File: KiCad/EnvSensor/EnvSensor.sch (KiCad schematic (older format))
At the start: 57 parts

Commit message: Schematic done
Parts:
- removed D?: WS2812B, LED_SMD:LED_WS2812B_PLCC4_5.0x5.0mm_P3.2mm, symbol LED:WS2812B
- added BZ?: Buzzer, symbol Device:Buzzer
- added C? (x2): 1u, symbol Device:C
- added C? (x4): 100n, symbol Device:C
- added D?: GREEN_LED, symbol Device:LED
- added Q?: IRLML2502, Package_TO_SOT_SMD:SOT-23, symbol Transistor_FET:IRLML2060
- added R?: 10, symbol Device:R
- added R? (x5): 100k, symbol Device:R
- added R?: 1m, symbol Device:R
- added R?: 2k2, symbol Device:R
- added R? (x4): 10k, symbol Device:R
- added SW? (x4): SW_Push, symbol Switch:SW_Push
- added U?: TPS782-DDC, Package_TO_SOT_SMD:SOT-23-5, symbol myLib:TPS782-DDC
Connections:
- net +3V3: now also BZ?.1 (-), J?.4 (VDD), U?.1 (VDD), U?.8 (VCC), R?.1, R?.1, R?.1, R?.1; no longer U?.1 (VDD)
- net +BATT: now also C?.1, U?.1 (VIN)
- net GND: now also J?.6 (VSS), U?.2 (GND), U?.9 (GND), C?.2, C?.2, C?.2, C?.2, C?.2, C?.2, Q?.2 (S), R?.2, R?.2, R?.2, SW?.1, SW?.1, SW?.1, SW?.1
- net MOSI: now reaches U?.3 (DIN)
- net MOSI: now also J?.3 (CMD)
- net SCK: now reaches U?.4 (CLK)
- net SCK: now also J?.5 (CLK)
- net E_INK_SELECT: now reaches U?.5 (CS)
- net E_INK_CD: now reaches U?.6 (DC)
- net E_INK_RESET: now reaches U?.7 (RST)
- net E_INK_BUSY: now reaches U?.8 (BUSY)
- net BUZZ_DAC: now reaches U?.15 (PA5)
- net at BZ?.2 (+): now also R?.1
- net SD_CS: now reaches J?.2 (DAT3/CD)
- net MISO: now reaches J?.7 (DAT0)
- net WIFI_RESET: now reaches U?.1 (Reset)
- net WIFI_RX: now reaches U?.15 (RXD0)
- net WIFI_TX: now reaches U?.16 (TXD0)
- net WIFI_ENABLE: now reaches U?.3 (EN)
- new net: Q?.3 (D), R?.2
- new net: D?.1 (K), R?.1
- new net: R?.2, R?.2, SW?.2 (x4)
- new net +3.3VP: C?.1, U?.1 (VDD), U?.5 (VOUT)
- new net AUX_POWER_ENABLE: R?.1, U?.3 (EN)
- new net BUZZ_SWITCH: Q?.1 (G), R?.1
- new net LED: D?.2 (A)
- new net SWITCH_1: C?.1, R?.1
- new net SWITCH_2: C?.1, R?.1
- new net SWITCH_3: C?.1, R?.1
- new net SWITCH_4: C?.1, R?.1
- no-connect marks 1 -> 13
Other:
- note added: "I(led)=1mA\nR=(3.3V-1.8V)/1mA\nR=1k5"
- note added: "SCD30 C02 sensor\n3.3-5.5V\n1-75mA, 20mA avg"
- note added: "STM32L431CCTx | MTU | | 1.71-3.6 V\nUSB connectivity?\n\nMCP73832 | USB Battery charger\nAP9101 | Battery protection\nTPS782 | 500-nA IQ,150-mA, Ultra-Low Quiescent Current\nLow-Dropout Linear Regulator\n\nSCD30 | C02 sensor | I2C 0xC2 | 3.3-5.5VV / 1-65mA, 20mA avg\nHIH8121 | Humidity | I2c 0x27 | 2.3-5.5V / 1mA\nBME280 | Pressure | I2C 0x76/0x77 | 1.7-3.6V\nSSD1306 | Display | I2C 0x3C << 1 | 3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"
- note added: "TPS782 LDO\nDropout 135-175mV\nImax 150-mA\n500-nA Quiescent Current\n"
- note added: "WiFi Module"
- note removed: "SCD30 C02 sensor\n"
- note removed: "STM32L431CCTx | MTU | | 1.71-3.6 V\nUSB connectivity?\n\nMCP73832 | USB Battery charger\nAP9101 | Battery protection\nTPS782 | 500-nA IQ,150-mA, Ultra-Low Quiescent Current\nLow-Dropout Linear Regulator\n\nSCD30 | C02 sensor | I2C 0xC2 | 3.3-5.5VV / 20mA\nHIH8121 | Humidity | I2c 0x27 | 2.3-5.5V / 1mA\nBME280 | Pressure | I2C 0x76/0x77 | 1.7-3.6V\nSSD1306 | Display | I2C 0x3C << 1 | 3.3V\n | Ink 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"
- note removed: "TPS782 LDO\n135-175mV\n150-mA\n500-nA Quiescent Current\n"
- moved on the sheet: BZ?, C?, D?, F?, J?, L?, Q?, Q?A, Q?B, R?, U?, Y?

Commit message: Some commit
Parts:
- removed BZ?: Buzzer, symbol Device:Buzzer
- removed F?: 1812L200/12DR, symbol Device:Polyfuse
- removed Q? (x2): Si7252DP, symbol myLib:Si7252DP
- removed U?: USBLC6-2SC6, Package_TO_SOT_SMD:SOT-23-6, symbol Power_Protection:USBLC6-2SC6
- removed U?: STM32L475RCT6, Package_QFP:LQFP-64_10x10mm_P0.5mm, symbol MCU_ST_STM32L4:STM32L475RCTx
- added BT1, BT2, BT3: Li-Ion, JPConnectors:BatteryHolder_Keystone_1042_1x18650, symbol Device:Battery_Cell
- added C26, C27: 15p, Capacitor_SMD:C_0805_2012Metric, symbol Device:C
- added D5: GREEN_LED, LED_THT:LED_D3.0mm, symbol Device:LED
- added D6, D7: RED LED, LED_THT:LED_D3.0mm_Horizontal_O3.81mm_Z10.0mm, symbol Device:LED
- added H1, H2, H3, H4: MountingHole, MountingHole:MountingHole_3.2mm_M3, symbol Mechanical:MountingHole
- added Q3: SQJB80EP, Package_SO:PowerPAK_SO-8_Dual, symbol myLib:SQJB80EP
- added Y2: 32768/12.5pF, Crystal:Crystal_SMD_MicroCrystal_CC7V-T1A-2Pin_3.2x1.5mm, symbol Device:Crystal_Small
- BZ1: renamed from BZ?; footprint (none) -> JPBuzzers:Laudity_SPB45
- C1, C2: renamed from C?; value 100n -> 6p; footprint (none) -> Capacitor_SMD:C_0805_2012Metric
- C10, C13, C14, C16, C19, C20, C3, C6, C7, C8, C9: renamed from C?; footprint (none) -> Capacitor_SMD:C_0603_1608Metric
- C11, C12, C17, C18, C21, C22, C23, C24, C25, C4: renamed from C?; footprint (none) -> Capacitor_SMD:C_0805_2012Metric
- C15: renamed from C?; value 10n -> 100n; footprint (none) -> Capacitor_SMD:C_0603_1608Metric
- C5: renamed from C?; value 100n -> 10n; footprint (none) -> Capacitor_SMD:C_0805_2012Metric
- D1, D3, D4: renamed from D?; footprint (none) -> LED_SMD:LED_0805_2012Metric
- D2: renamed from D?; value D -> MBRS260T3G; footprint (none) -> Diode_SMD:D_SMB
- J1: renamed from J?; footprint (none) -> Connector_PinHeader_2.54mm:PinHeader_1x06_P2.54mm_Horizontal
- J2: renamed from J?; footprint (none) -> Connector_PinSocket_2.54mm:PinSocket_1x04_P2.54mm_Vertical
- J3: renamed from J?; footprint (none) -> Connector_USB:USB_Micro-B_Molex_47346-0001
- J4: renamed from J?; footprint (none) -> JPConnectors:PowerSocketSMD
- J5: renamed from J?; footprint (none) -> Connector_Card:microSD_HC_Hirose_DM3AT-SF-PEJM5
- L1: renamed from L?; value L_Small -> 10u; footprint (none) -> Inductor_SMD:L_0805_2012Metric
- P1: renamed from P?; footprint (none) -> Connector_USB:USB_C_Receptacle_Amphenol_12401610E4-2A
- R1, R11, R14, R16, R20, R3, R4, R8: renamed from R?; footprint (none) -> Resistor_SMD:R_0805_2012Metric
- R10, R12, R13, R15, R18, R19, R2, R6, R7, R9: renamed from R?; footprint (none) -> Resistor_SMD:R_0603_1608Metric
- R17: renamed from R?; footprint (none) -> Resistor_SMD:R_2512_6332Metric
- R21: renamed from R?; value 1m -> 300k; footprint (none) -> Resistor_SMD:R_0805_2012Metric
- R5: renamed from R?; value 10 -> 100; footprint (none) -> Resistor_SMD:R_0805_2012Metric
- SW1, SW2, SW3, SW4: renamed from SW?; footprint (none) -> Button_Switch_SMD:SW_SPST_PTS645
- U1: renamed from U?; value STM32L431CCTx -> STM32L431CCT6
- U10: renamed from U?; footprint (none) -> JPSensors:BME280-Module
- U11: renamed from U?; footprint (none) -> JPDisplays:4.2inch_E-Ink
- U2: renamed from U?; footprint (none) -> Package_SO:MSOP-8_3x3mm_P0.65mm
- U5: renamed from U?; footprint (none) -> JPSensors:SCD30
- U8: renamed from U?; footprint (none) -> Connector_PinHeader_1.27mm:PinHeader_1x04_P1.27mm_Vertical
- U9: renamed from U?; footprint (none) -> JPComms:ESP-12S
- Y1: renamed from Y?; footprint (none) -> Crystal:Crystal_SMD_Abracon_ABM3B-4Pin_5.0x3.2mm
- gave numbers to parts that had none: 6
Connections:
- net BUZZ_DAC is gone; now on net E_INK_RESET: U1.15 (PA5)
- net +3V3: now also U4.6 (VDDIO), U4.8 (VDD); no longer U4.1 (GND), U4.7 (GND)
- net +BATT: now also BT1.1 (+), BT2.1 (+), BT3.1 (+)
- net -BATT: now also BT1.2 (-), BT2.2 (-), BT3.2 (-), Q3.3 (S2)
- net AUX_POWER_ENABLE: now also U1.33 (PA12)
- net BUZZ_SWITCH: now also U1.25 (PB12)
- net E_INK_BUSY: now also U1.16 (PA6)
- net E_INK_CD: now also U1.14 (PA4)
- net E_INK_SELECT: now also U1.13 (PA3)
- net GND: now also U1.44 (PH3), U4.1 (GND), U4.7 (GND), U6.2 (GND), U6.4 (GND), U7.2 (GND), U7.4 (GND), C26.2, C27.2, Q3.1 (S2); no longer U4.6 (VDDIO), U4.8 (VDD)
- net LED: now also U1.22 (PB11), D5.2 (A)
- net MISO: now also U1.27 (PB14)
- net MOSI: now also U1.28 (PB15)
- net SCD30_READY: now also U1.32 (PA11)
- net SCK: now also U1.26 (PB13)
- net SCL: now also U1.30 (PA9), U4.4 (SCK); no longer U4.3 (SDI)
- net SDA: now also U1.31 (PA10), U4.3 (SDI); no longer U4.4 (SCK)
- net SD_CS: now also U1.29 (PA8)
- net SWITCH_1: now also U1.17 (PA7)
- net SWITCH_2: now also U1.18 (PB0)
- net SWITCH_3: now also U1.19 (PB1)
- net SWITCH_4: now also U1.20 (PB2)
- net VBUS: now also D2.2 (A), D7.2 (A)
- net WIFI_ENABLE: now also U1.46 (PB9)
- net WIFI_RESET: now also U1.45 (PB8)
- net WIFI_RX: now also U1.42 (PB6)
- net WIFI_TX: now also U1.43 (PB7)
- net at U1.3 (PC14): now also C26.1, Y2.1
- net at U1.4 (PC15): now also C27.1, Y2.2
- net at U3.4 (DO): now also Q3.4 (G2)
- net at U3.5 (CO): now also Q3.2 (G2)
- net at P1.A6 (D+): no longer J3.3 (D+)
- net at P1.A7 (D-): no longer J3.2 (D-)
- net at C11.1, D2.1 (K), D3.2 (A)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: now also D6.2 (A)
- net at D4.1 (K), R20.2: now also D7.1 (K)
- net at D3.1 (K), R11.2: now also D6.1 (K)
- net at D1.1 (K), R4.1: now also D5.1 (K)
- new net: Q3.5 (D2), Q3.6 (D2)
- no-connect marks 13 -> 30
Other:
- note added: "Boot?"
- note added: "C1/2 = 2C(L) - 10p\nC(L)=12.5p -> C1/2=15p\nC(L)=9p -> C1/2=8p\nC(L)=7p -> C1/2=4p\n"
- note added: "I(buzz)=5mA\nRmax=3.3V/5mA\nRmax=660"
- note added: "Settings\n+\n-\nAlarm\nPower save mode\nTrigger gps"
- note added: "TPS782 LDO\nDropout 135-175mV\nImax 150-mA\n500-nA Quiescent Current"
- note added: "deltaT=(5.0V-0.5V-3.3V)*65mA*193C/W\ndeltaT=78mW*193C/W=15C"
- note removed: "TPS782 LDO\nDropout 135-175mV\nImax 150-mA\n500-nA Quiescent Current\n"
- moved on the sheet: BZ1, C1, C10, C12, C15, C2, C4, C5, C6, C7, C9, D1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

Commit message: Last pcb fixes
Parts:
- P1: footprint Connector_USB:USB_C_Receptacle_Amphenol_12401610E4-2A -> JPConnectors:USB_C_Receptacle_Adam_Tech
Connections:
- net VBUS: no longer D4.2 (A), D7.2 (A)
- net at C11.1, D2.1 (K), D3.2 (A)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: now also D4.2 (A), D7.2 (A)
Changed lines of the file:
@@
 F 0 "P1" H 1807 3467 50  0000 C CNN
 F 1 "USB_C_Plug_USB2.0" H 1807 3376 50  0000 C CNN
-F 2 "Connector_USB:USB_C_Receptacle_Amphenol_12401610E4-2A" H 1850 2600 50  0001 C CNN
+F 2 "JPConnectors:USB_C_Receptacle_Adam_Tech" H 1850 2600 50  0001 C CNN
 F 3 "https://www.usb.org/sites/default/files/documents/usb_type-c.zip" H 1850 2600 50  0001 C CNN
 	1    1700 2600
@@
 $EndComp
 $Comp
-L power:VBUS #PWR0110
-U 1 1 5F7F80CF
-P 7150 4850
-F 0 "#PWR0110" H 7150 4700 50  0001 C CNN
-F 1 "VBUS" H 7165 5023 50  0000 C CNN
-F 2 "" H 7150 4850 50  0001 C CNN
-F 3 "" H 7150 4850 50  0001 C CNN
-	1    7150 4850
-	0    1    1    0
-$EndComp
-$Comp
 L Device:C C11
 U 1 1 5F7F94C0
@@
 	4600 3950 4900 3950
 Wire Wire Line
-	4900 3950 4900 4700
+	4900 3950 4900 4150
 Connection ~ 4900 3950
 Wire Wire Line
@@
 Wire Wire Line
 	7100 4700 7050 4700
-Connection ~ 7100 4850
-Wire Wire Line
-	7100 4850 7150 4850
 Wire Wire Line
 	9700 2250 9700 2300
@@
 Text Notes 10650 3800 0    50   ~ 0
 deltaT=(5.0V-0.5V-3.3V)*65mA*193C/W\ndeltaT=78mW*193C/W=15C
+Wire Wire Line
+	7100 4700 7100 4150
+Wire Wire Line
+	7100 4150 4900 4150
+Connection ~ 7100 4700
+Connection ~ 4900 4150
+Wire Wire Line
+	4900 4150 4900 4700
 $EndSCHEMATC

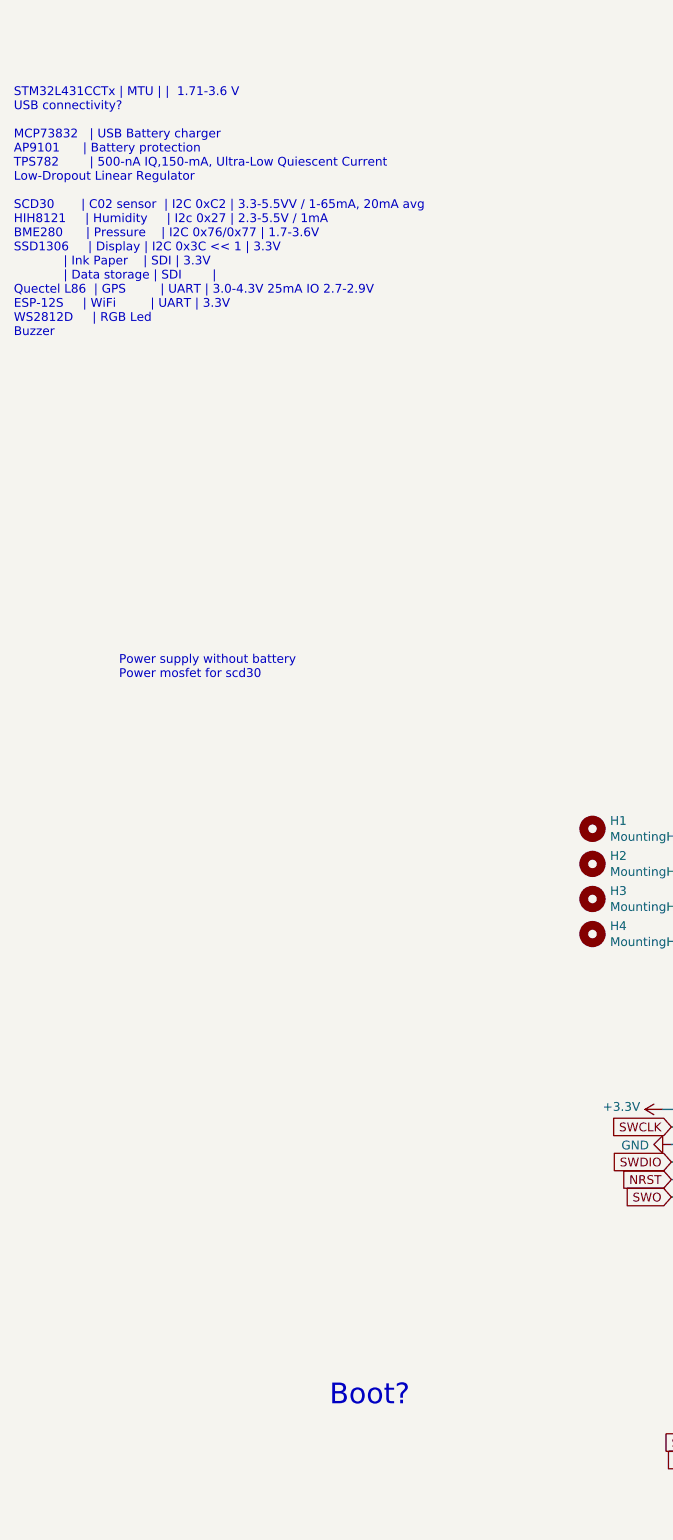
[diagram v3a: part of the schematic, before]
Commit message: SCD30 code added
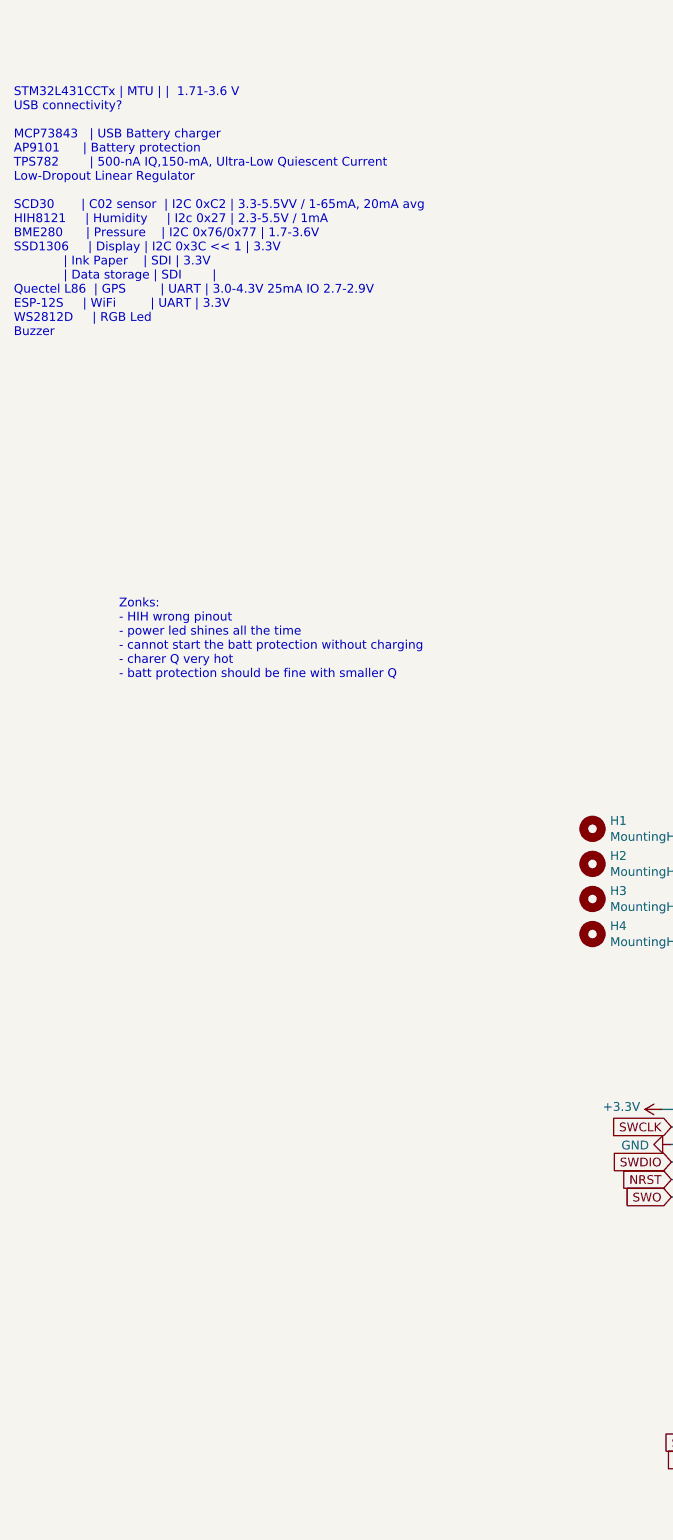
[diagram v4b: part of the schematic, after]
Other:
- note added: "STM32L431CCTx | MTU | | 1.71-3.6 V\nUSB connectivity?\n\nMCP73843 | USB Battery charger\nAP9101 | Battery protection\nTPS782 | 500-nA IQ,150-mA, Ultra-Low Quiescent Current\nLow-Dropout Linear Regulator\n\nSCD30 | C02 sensor | I2C 0xC2 | 3.3-5.5VV / 1-65mA, 20mA avg\nHIH8121 | Humidity | I2c 0x27 | 2.3-5.5V / 1mA\nBME280 | Pressure | I2C 0x76/0x77 | 1.7-3.6V\nSSD1306 | Display | I2C 0x3C << 1 | 3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"
- note added: "Zonks:\n- HIH wrong pinout\n- power led shines all the time\n- cannot start the batt protection without charging\n- charer Q very hot\n- batt protection should be fine with smaller Q"
- note removed: "Boot?"
- note removed: "Power supply without battery\nPower mosfet for scd30"
- note removed: "STM32L431CCTx | MTU | | 1.71-3.6 V\nUSB connectivity?\n\nMCP73832 | USB Battery charger\nAP9101 | Battery protection\nTPS782 | 500-nA IQ,150-mA, Ultra-Low Quiescent Current\nLow-Dropout Linear Regulator\n\nSCD30 | C02 sensor | I2C 0xC2 | 3.3-5.5VV / 1-65mA, 20mA avg\nHIH8121 | Humidity | I2c 0x27 | 2.3-5.5V / 1mA\nBME280 | Pressure | I2C 0x76/0x77 | 1.7-3.6V\nSSD1306 | Display | I2C 0x3C << 1 | 3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"
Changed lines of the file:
@@
 $EndDescr
 Text Notes -2550 2000 0    50   ~ 0
-STM32L431CCTx | MTU | |  1.71-3.6 V\nUSB connectivity?\n\nMCP73832   | USB Battery charger\nAP9101      | Battery protection\nTPS782        | 500-nA IQ,150-mA, Ultra-Low Quiescent Current\nLow-Dropout Linear Regulator\n\nSCD30       | C02 sensor  | I2C 0xC2 | 3.3-5.5VV / 1-65mA, 20mA avg\nHIH8121     | Humidity     | I2c 0x27 | 2.3-5.5V / 1mA\nBME280      | Pressure    | I2C 0x76/0x77 | 1.7-3.6V\nSSD1306     | Display | I2C 0x3C << 1 | 3.3V\n             | Ink Paper    | SDI | 3.3V\n             | Data storage | SDI        | \nQuectel L86  | GPS         | UART | 3.0-4.3V 25mA IO 2.7-2.9V\nESP-12S     | WiFi         | UART | 3.3V\nWS2812D     | RGB Led\nBuzzer\n
+STM32L431CCTx | MTU | |  1.71-3.6 V\nUSB connectivity?\n\nMCP73843   | USB Battery charger\nAP9101      | Battery protection\nTPS782        | 500-nA IQ,150-mA, Ultra-Low Quiescent Current\nLow-Dropout Linear Regulator\n\nSCD30       | C02 sensor  | I2C 0xC2 | 3.3-5.5VV / 1-65mA, 20mA avg\nHIH8121     | Humidity     | I2c 0x27 | 2.3-5.5V / 1mA\nBME280      | Pressure    | I2C 0x76/0x77 | 1.7-3.6V\nSSD1306     | Display | I2C 0x3C << 1 | 3.3V\n             | Ink Paper    | SDI | 3.3V\n             | Data storage | SDI        | \nQuectel L86  | GPS         | UART | 3.0-4.3V 25mA IO 2.7-2.9V\nESP-12S     | WiFi         | UART | 3.3V\nWS2812D     | RGB Led\nBuzzer\n
 $Comp
 L myLib:SCD30 U5
@@
 $EndComp
 Text Notes -1950 3950 0    50   ~ 0
-Power supply without battery\nPower mosfet for scd30
+Zonks:\n- HIH wrong pinout\n- power led shines all the time\n- cannot start the batt protection without charging\n- charer Q very hot\n- batt protection should be fine with smaller Q
 $Comp
 L power:+3.3V #PWR0137
@@
 	1350 9450 1350 9500
 Connection ~ 1350 9500
-Text Notes -750 8100 0    118  ~ 0
-Boot?
 NoConn ~ 5400 9750
 Wire Wire Line
